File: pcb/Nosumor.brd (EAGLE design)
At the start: 50 x 50 mm, 111 parts, among them IC1 STM32F722RET, IC2 REG1117, IC3 TPS77018, J3 SJ-43515TS-SMT-EDGE, K1 CHERRY-MX, K2 CHERRY-MX, K3 KSC623J, K4 KSC623J, K5 KSC623J, Q1 CX2016DB, Q2 ABMM-6.000MHZ, Q3 FDY100PZ, Q4 FDY100PZ, Q5 FDY100PZ, Q6 FDY100PZ, U2 USB3370, U3 TLV320AIC3110

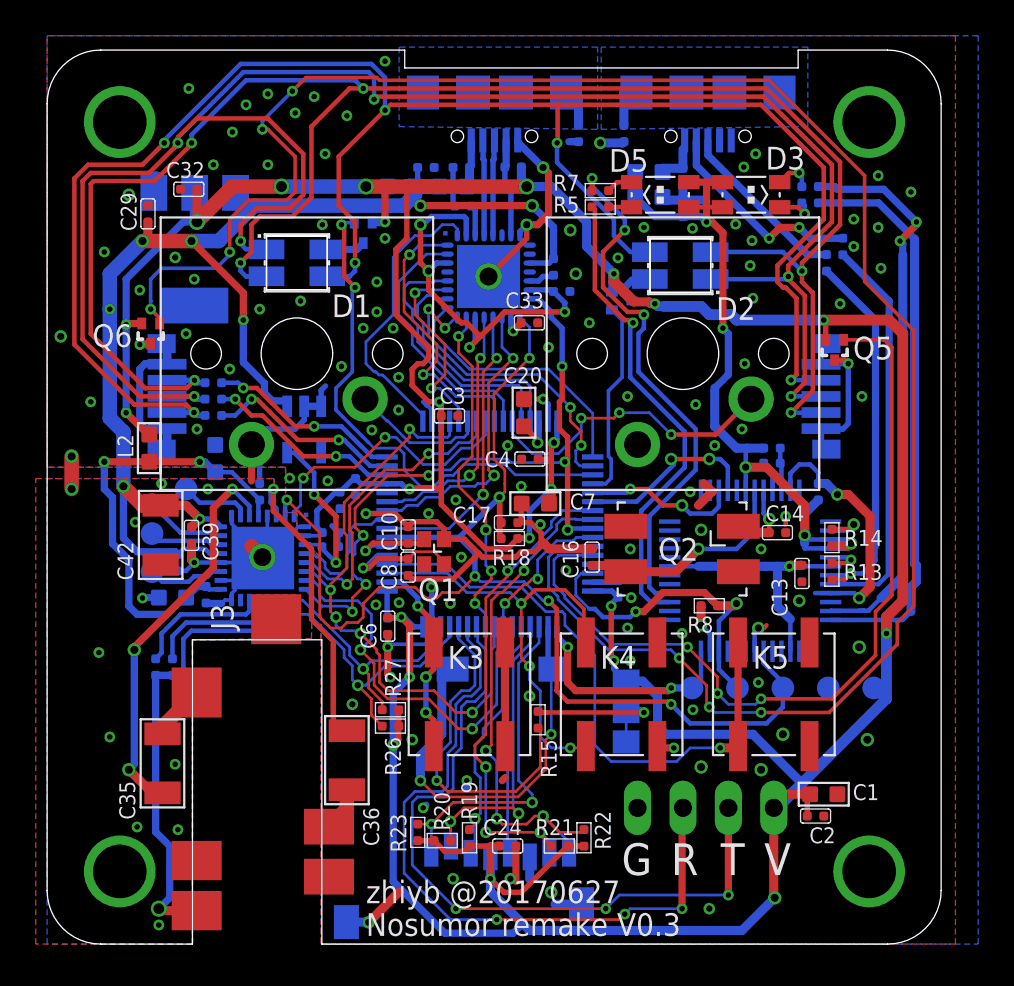
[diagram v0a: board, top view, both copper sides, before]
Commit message: PCB: Connections done, update revision to 1.0
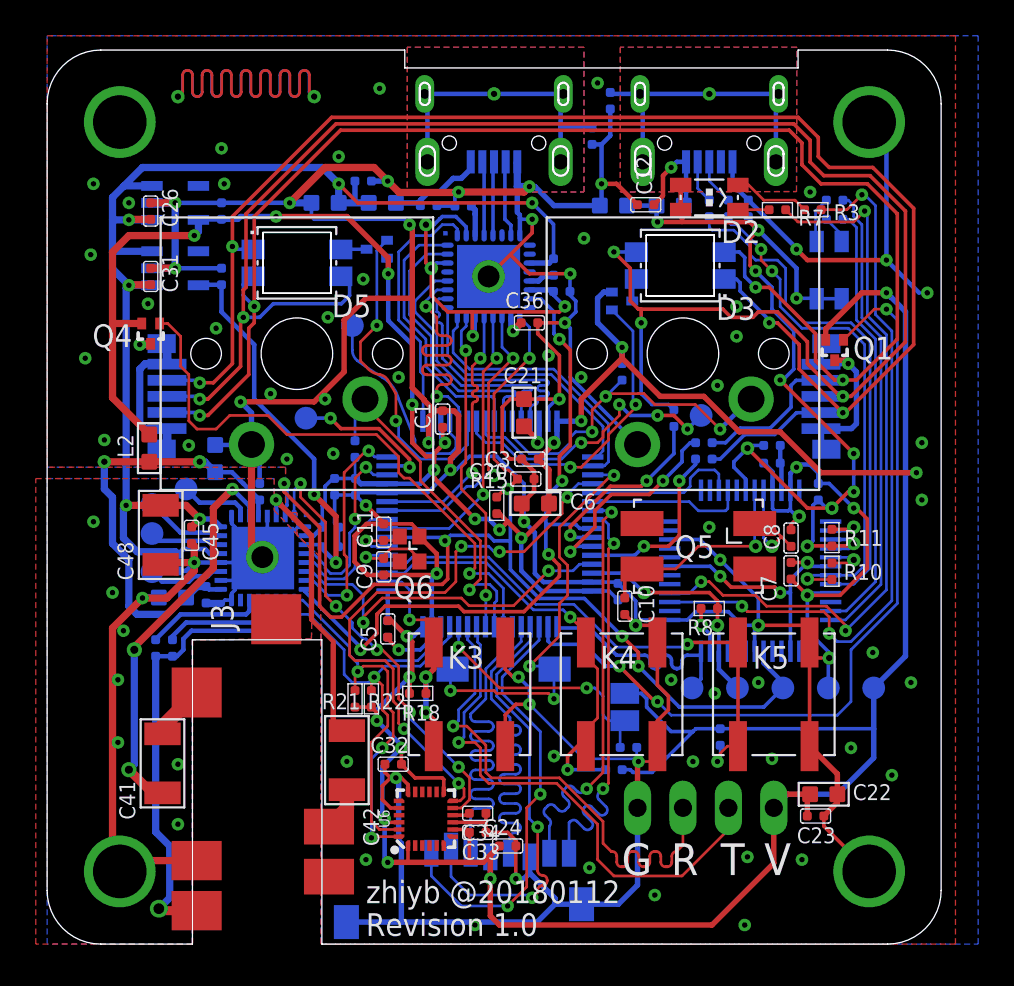
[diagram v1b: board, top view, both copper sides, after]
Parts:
- removed BOOT: 0R-JUMPB, jump-0r-smd:B0R-JMP
- removed IC2: REG1117, burr-brown:SOT223
- removed IC3: TPS77018, texas:SOT23-DBV
- removed R26, R27, R31: 2.2K, Seeed-Resistor:R0402
- removed R28, R30: 10K 1/16W, Seeed-Resistor:R0402
- added A1, A2, D: TPB1,27, testpad:B1,27
- added C45, C46, C47, C49: 100nf, Seeed-Capacitor:C0402
- added C48: 100uf, Seeed-Capacitor:C1206
- added R1, R3: 330R, Seeed-Resistor:R0402
- added R2: 150R, Seeed-Resistor:R0402
- added R25: 2.2K, Seeed-Resistor:R0402
- added SJ1: (no value), jumper:SJ
- added U4: TLV320AIC3110, ti:VQFN32
- added U5: AP2112K-1.8V, SparkFun-IC-Power:SOT23-5
- added U6: 9DoF IMU, SparkFun-Sensors:QFN24-3X3
- C1, C23, C27, C37: value 10uf -> 100nf; device Seeed-Capacitor:C0603 -> Seeed-Capacitor:C0402
- C10, C8: value 12pf -> 18pf
- C11: value 10nf -> 12pf
- C12: value 1UF 6.3V -> 100nf
- C13: value 33nf -> 100nf
- C14: value 18pf -> 10nf
- C16: value 18pf -> 100nf
- C17, C26, C31, C38: value 100nf -> 1UF 6.3V
- C18, C22, C28, C43, C44: value 100nf -> 10uf; device Seeed-Capacitor:C0402 -> Seeed-Capacitor:C0603
- C20: value 4.7uf -> 100nf; device Seeed-Capacitor:C0603 -> Seeed-Capacitor:C0402
- C21, C6: value 100nf -> 4.7uf; device Seeed-Capacitor:C0402 -> Seeed-Capacitor:C0603
- C33: value 1UF 6.3V -> 10nf
- C34: value 470nf -> 100nf
- C35, C36: value 100uf -> 1UF 6.3V; device Seeed-Capacitor:C1206 -> Seeed-Capacitor:C0402
- C40: value 10uf -> 470nf; device Seeed-Capacitor:C0603 -> Seeed-Capacitor:C0402
- C41: value 100nf -> 100uf; device Seeed-Capacitor:C0402 -> Seeed-Capacitor:C1206
- C7: value 4.7uf -> 33nf; device Seeed-Capacitor:C0603 -> Seeed-Capacitor:C0402
- C9: value 100nf -> 12pf
- D1, D2: value HSMF-A3-BACK -> APBD3224SURKCGKC-F01; device led:HSMF-A3-BACK -> led:1210
- D3, D5: value APBD3224SURKCGKC-F01 -> HSMF-A3-BACK; device led:1210 -> led:HSMF-A3-BACK
- J1, J4: device Wurth_Elektronik_Electromechanic_Input-Output_Connectors_rev17b:629105136821 -> Wurth_Elektronik_Electromechanic_Input-Output_Connectors_rev16b:629105150521
- Q1: value CX2016DB -> FDY100PZ; device crystal:CX2016DB -> transistor:SC-89
- Q2: value ABMM-6.000MHZ -> FDY100PZ; device crystal:ABMM -> transistor:SC-89
- Q5: value FDY100PZ -> ABMM-6.000MHZ; device transistor:SC-89 -> crystal:ABMM
- Q6: value FDY100PZ -> CX2016DB; device transistor:SC-89 -> crystal:CX2016DB
- R10: value 150R -> 1.5K
- R11: value 150R -> 10K 1/16W
- R12: value 150R -> 22R
- R13: value 1.5K -> 22R
- R16, R17: value 22R -> 10K 1/16W
- R19, R20, R23: value 47K -> 10K 1/16W
- R21, R22: value 47K -> 2.2K
- R4, R6: value 330R -> 150R
- U2: value USB3370 -> AP2112K-3.3V; device microchip:QFN32 -> SparkFun-IC-Power:SOT23-5
- U3: value TLV320AIC3110 -> USB3370; device ti:VQFN32 -> microchip:QFN32
- moved R10 36.2 mm to (43.9, 20.9), flipped to the top, turned to 0 degrees
- moved C23 35.9 mm to (43.0, 7.16), flipped to the top, turned to 270 degrees
- moved R11 35.5 mm to (43.9, 22.7), flipped to the top, turned to 0 degrees
- moved R23 35.1 mm to (23.3, 41.3), flipped to the bottom, turned to 270 degrees
- moved C35 34.6 mm to (28.8, 36.5), flipped to the bottom
- moved C32 34.1 mm to (19.4, 10.1)
- moved C15 31.9 mm to (31.5, 47.2)
- moved R12 30.1 mm to (37.0, 41.1), turned to 180 degrees
- moved C1 29.9 mm to (22.1, 29.4), turned to 0 degrees
- moved D1 29.8 mm to (43.7, 37.7), flipped to the bottom, turned to 0 degrees
- moved R16 29.5 mm to (17.2, 27.7), turned to 0 degrees
- moved C40 29.2 mm to (6.07, 16.6), turned to 0 degrees
- moved C19 28.7 mm to (19.1, 17.6), turned to 180 degrees
- moved C33 28.6 mm to (24.1, 6.25)
- moved C36 26.5 mm to (27.0, 34.7)
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- renumbered 3V3 to VDD, R29 to R24, SLM to TP10, SLP to TP9, SRM to TP12, SRP to TP11, UART to JP1
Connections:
- removed net AIC_SCL: IC1.61, R26.1, U3.10
- removed net AIC_SDA: IC1.62, R27.1, U3.9
- removed net N$15: R16.1, U1.8
- removed net N$16: J1.3, R17.2
- removed net N$22: C21.2, J1.SHELL, J1.SHELL1, J1.SHELL2, J1.SHELL3
- removed net N$40: D1.3, D2.3, D4.5, D6.5, R12.2
- removed net N$41: D1.1, D2.1, D4.4, D6.4, R11.2
- removed net N$42: D1.4, D2.4, D4.3, D6.3, R10.2
- removed net N$51: C27.2, C28.2, C31.2, C37.2, L2.1, U3.17, U3.28
- removed net N$8: J1.2, R16.2
- removed net N$9: R13.2, R17.1, U1.7
- removed net NC1: IC1.45
- removed net RGB2_B: IC1.16, R10.1
- removed net RGB2_G: IC1.15, R12.1
- removed net RGB2_R: IC1.14, R11.1
- new net ADC1: A1.TP, IC1.15
- new net ADC2: A2.TP, IC1.24
- new net AVDD: C28.2, C29.2, C37.2, C43.2, L2.1, U4.17, U4.28
- new net DAC: D.TP, IC1.20
- new net DBG_BM_U: J1.2, R12.2
- new net DBG_DM: R12.1, U1.8
- new net DBG_DP: R10.2, R13.1, U1.7
- new net DBG_DP_U: J1.3, R13.2
- new net I2C_SCL: IC1.61, R21.1, U4.10, U6.23
- new net I2C_SDA: IC1.62, R22.1, U4.9, U6.24
- new net LED_B: IC1.44, R2.1
- new net LED_G: IC1.43, R6.1
- new net LED_R: IC1.42, R4.1
- new net MPU_INT: IC1.36, U6.12
- new net N$47: C34.2, U6.10
- new net RGB_B: D3.1, D4.3, D5.1, D6.3, R2.2
- new net RGB_G: D3.4, D4.5, D5.4, D6.5, R6.2
- new net RGB_R: D3.3, D4.4, D5.3, D6.4, R4.2
- net +1V8: now also C27.2, C38.2, U4.3, U5.5; no longer C26.2, IC3.5, U3.3
- net +3V3: now also C14.2, C17.2, C19.2, C22.2, C23.2, C30.2, C33.2, Q1.3, Q2.3, R15.2, R16.2, R17.2, R21.2, R22.2, SJ1.1, U2.5, U4.2, U6.1, U6.13, U6.22, U6.8; no longer BOOT.1, C11.2, C12.2, C15.2, C2.2, C7.2, IC2.2, Q5.3, Q6.3, R21.1, R22.1, R23.2, R26.2, R27.2, R30.2, U3.2
- net +5V: now also C26.2, C31.2, C44.2, C45.2, C46.2, C48.2, U2.1, U2.3, U3.11, U4.21, U4.24, U5.1, U5.3; no longer C29.2, C38.2, C40.2, C41.2, C42.2, IC2.3, IC3.1, U2.11, U3.21, U3.24
- net AIC_BCLK: now also IC1.16, U4.7; no longer IC1.42, IC1.55, U3.7
- net AIC_DIN: now also IC1.9, U4.5; no longer IC1.23, U3.5
- net AIC_DOUT: now also IC1.14, U4.4; no longer IC1.9, U3.4
- net AIC_GPIO: now also U4.32, U6.11; no longer IC1.24, U3.32
- net AIC_WCLK: now also IC1.45, U4.6; no longer IC1.20, IC1.56, U3.6
- net BOOT0: now also R14.1, SJ1.2; no longer R15.1
- net DBG_5V: now also C13.2, C16.2, C18.2, D1.1, D1.3, D2.1, D2.3, R11.2; no longer C19.2, C22.2, C23.2, D3.1, D3.3, D5.1, D5.3, R14.2
- net DBG_SWD_LED1: now also R5.1; no longer R6.1
- net DBG_SWD_LED2: now also R1.1; no longer R4.1
- net DBG_TX_LED: now also R3.1; no longer R5.1
- net GND: now also C13.1, C2.2, C34.1, C35.1, C36.1, C45.1, C46.1, C47.1, C48.1, C49.1, C7.2, C9.1, Q6.2, R14.2, R23.1, U2.2, U3.8, U4.1, U4.16, U4.18, U4.20, U4.25, U4.29, U4.EXP, U5.2, U6.18, U6.20, U6.9; no longer BOOT.3, C13.2, C2.1, C40.1, C41.1, C42.1, C7.1, C9.2, IC2.1, IC3.2, IC3.3, Q1.2, R28.1, U2.8, U2.EXP, U3.1, U3.16, U3.18, U3.20, U3.25, U3.29
- net KEY_1: now also IC1.56, R16.1; no longer IC1.22
- net KEY_2: now also R17.1
- net KEY_3: now also R18.1
- net KEY_4: now also R19.1
- net KEY_5: now also R20.1
- net LED_1: now also IC1.22; no longer IC1.35
- net LED_2: now also IC1.23, Q2.1; no longer IC1.36, Q4.1
- net LED_3: now also IC1.50, Q1.1; no longer IC1.44, Q5.1
- net LED_4: now also IC1.55, Q4.1; no longer IC1.43, Q6.1
- net MCLK: now also U3.15, U4.8; no longer U2.15, U3.8
- net MMC_CD: now also IC1.35; no longer IC1.50
- net MMC_CMD: no longer R19.1
- net MMC_D0: no longer R21.2
- net MMC_D1: no longer R22.2
- net MMC_D2: no longer R23.1
- net MMC_D3: no longer R20.1
- net N$1: now also C41.2; no longer C35.2
- net N$10: now also C7.1; no longer C13.1
- net N$11: now also C2.1; no longer C9.1
- net N$12: now also D1.4, R5.2; no longer D3.4, R6.2
- net N$13: now also C12.2; no longer C18.2
- net N$14: now also R10.1; no longer R13.1
- net N$17: now also R11.1; no longer R14.1
- net N$18: now also C8.2, Q5.1; no longer C14.2, Q2.1
- net N$19: now also C10.2, Q5.3; no longer C16.2, Q2.3
- net N$2: now also C42.2; no longer C36.2
- net N$20: now also D2.4; no longer D5.4
- net N$21: now also D2.2, R3.2; no longer D5.2, R5.2
- net N$23: now also D1.2, R1.2; no longer D3.2, R4.2
- net N$24: now also C9.2, Q6.1; no longer C8.2, Q1.1
- net N$26: now also C11.2, Q6.3; no longer C10.2, Q1.3
- net N$27: now also C15.2, J1.Z1, J1.Z2, J1.Z3, J1.Z4; no longer BOOT.2, R15.2
- net N$28: now also Q4.2; no longer Q6.2
- net N$29: now also C21.2; no longer C20.2
- net N$3: now also C40.2, R25.2, U4.11; no longer C34.2, R31.2, U3.11
- net N$30: now also U4.19; no longer U3.19
- net N$31: now also C47.2; no longer C43.2
- net N$32: now also U3.13; no longer U2.13
- net N$33: now also C35.2, U3.14, U3.2, U3.22, U3.30; no longer C30.2, U2.14, U2.2, U2.22, U2.30
- net N$34: now also D5.2; no longer D1.2
- net N$35: now also C49.2, J4.Z1, J4.Z2, J4.Z3, J4.Z4; no longer C44.2, J4.SHELL, J4.SHELL1, J4.SHELL2, J4.SHELL3
- net N$36: now also C36.2, U3.18; no longer C33.2, U2.18
- net N$37: now also R23.2, U3.3; no longer R28.2, U2.3
- net N$38: now also Q1.2; no longer Q5.2
- net N$39: now also D3.2, Q2.2; no longer D2.2, Q4.2
- net N$4: now also J4.2, U3.4; no longer J4.3, U2.5
- net N$44: now also U4.26; no longer U3.26
- net N$45: now also U4.23; no longer U3.23
- net N$46: now also C40.1, U4.14; no longer C34.1, U3.14
- net N$48: now also C42.1, U4.30; no longer C36.1, U3.30
- net N$49: now also R25.1, U4.12; no longer R31.1, U3.12
- net N$5: now also J4.3, U3.5; no longer J4.2, U2.4
- net N$50: now also C41.1, U4.27; no longer C35.1, U3.27
- net N$6: now also U3.7; no longer R30.1, U2.7
- net N$7: now also U4.22; no longer U3.22
- net SRST_N: now also C20.2, R15.1, U3.17, U4.31; no longer C17.2, R18.1, U2.17, U3.31
- net ULPI_CLK: now also U3.27; no longer U2.27
- net ULPI_D0: now also U3.1; no longer U2.1
- net ULPI_D1: now also U3.32; no longer U2.32
- net ULPI_D2: now also U3.31; no longer U2.31
- net ULPI_D3: now also U3.28; no longer U2.28
- net ULPI_D4: now also U3.26; no longer U2.26
- net ULPI_D5: now also U3.25; no longer U2.25
- net ULPI_D6: now also U3.24; no longer U2.24
- net ULPI_D7: now also U3.23; no longer U2.23
- net ULPI_DIR: now also U3.19; no longer U2.19
- net ULPI_NXT: now also U3.21; no longer U2.21
- net ULPI_STP: now also U3.20; no longer U2.20
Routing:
- net GND: track 131.7 -> 414.5 mm, vias 129 -> 98
- net N$40: track 106.6 -> 0.00 mm, vias 6 -> 0
- net N$41: track 104.7 -> 0.00 mm, vias 6 -> 0
- net N$42: track 103.4 -> 0.00 mm, vias 6 -> 0
- net RGB_R: track 0.00 -> 102.6 mm, vias 0 -> 5
- net RGB_B: track 0.00 -> 89.3 mm, vias 0 -> 4
- net RGB_G: track 0.00 -> 89.1 mm, vias 0 -> 4
- net LED_4: track 112.6 -> 32.7 mm, vias 7 -> 1
- net N$22: track 2.52 -> 47.7 mm, vias 0 -> 2
- net MPU_INT: track 0.00 -> 32.6 mm, vias 0 -> 5
- net DBG_DP: track 0.00 -> 29.3 mm, vias 0 -> 3
- net DBG_DM: track 0.00 -> 28.9 mm
- net I2C_SDA: track 0.00 -> 26.2 mm, vias 0 -> 3
- net N$51: track 25.2 -> 0.00 mm, vias 2 -> 0
- net AVDD: track 0.00 -> 25.2 mm, vias 0 -> 2
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- added copper zone on layer 1, net N$27
- added copper zone on layer 16, net N$27
- added copper zone on layer 1, net N$35
- removed copper zone on layer 16, net N$22
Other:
- board text added: "Revision 1.0"
- board text added: "zhiyb @20180112"
- board text removed: "Nosumor remake V0.3"
- board text removed: "OwO"
- board text removed: "zhiyb @20170627"

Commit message: PCB: Revision 1.0, silkscreen checked
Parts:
- removed TP11, TP12: TPB1,27, testpad:B1,27
- added GND$2, SCL, SDA, SRM, SRP: TPB1,27, testpad:B1,27
- moved C28 0.61 mm to (6.40, 19.4)
- moved C29 0.36 mm to (8.53, 19.5)
- moved C43 0.30 mm to (9.09, 27.2)
- moved R20 0.30 mm to (37.3, 11.6)
- renumbered SJ1 to BOOT, TP10 to SLM, TP9 to SLP
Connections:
- net GND: now also GND$2.TP
- net I2C_SCL: now also SCL.TP
- net I2C_SDA: now also SDA.TP
- net N$44: now also SRP.TP; no longer TP11.TP
- net N$45: now also SRM.TP; no longer TP12.TP
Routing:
- net I2C_SDA: track 26.2 -> 34.4 mm, vias 3 -> 4
- net I2C_SCL: track 25.1 -> 33.3 mm, vias 1 -> 2
- net GND: track 414.5 -> 417.1 mm, vias 98 -> 102
- net KEY_3: track 12.7 -> 11.8 mm, vias 3 -> 2
- net AVDD: track 25.2 -> 25.8 mm
- net UART_TX: track 29.6 -> 29.1 mm
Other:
- board text added: "C"
- board text added: "D"

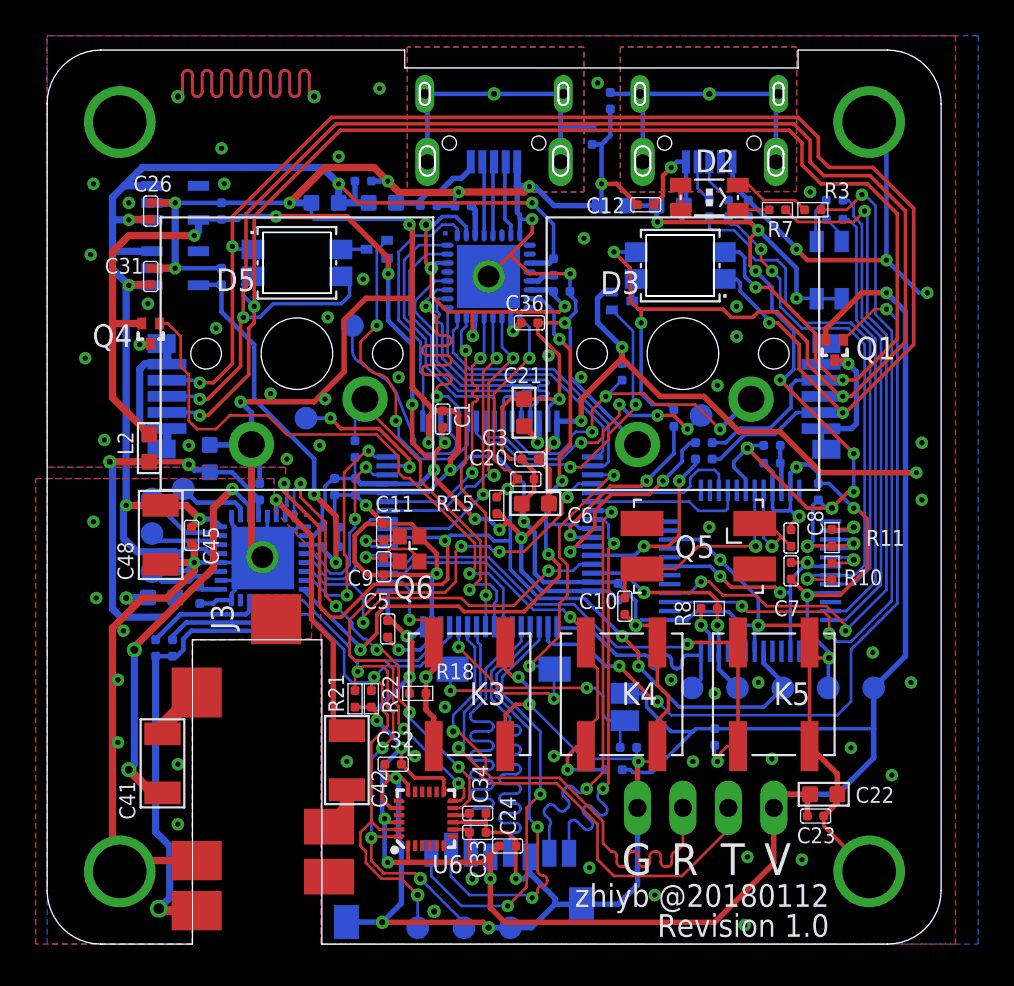
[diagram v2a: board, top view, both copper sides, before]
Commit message: PCB: Move a few things around (power supply rails)
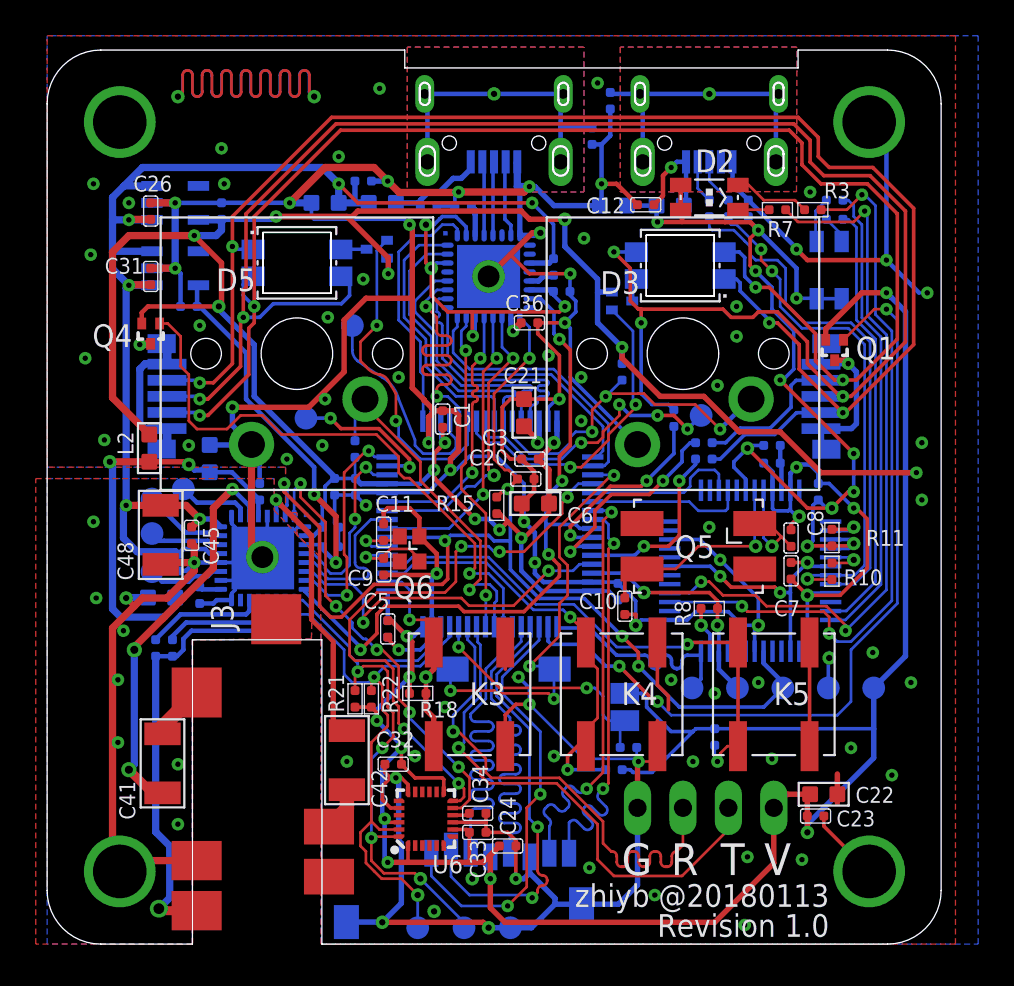
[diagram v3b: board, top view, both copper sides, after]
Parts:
- moved C38 2.48 mm to (7.92, 35.7), turned to 270 degrees
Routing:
- net +3V3: track 241.7 -> 267.4 mm, vias 21 -> 22
- net GND: track 417.1 -> 402.0 mm
- net AIC_DIN: track 7.52 -> 8.86 mm
- net +1V8: track 21.9 -> 21.3 mm
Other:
- board text added: "zhiyb @20180113"
- board text removed: "zhiyb @20180112"

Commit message: PCB: Conform to a more restrict design rule
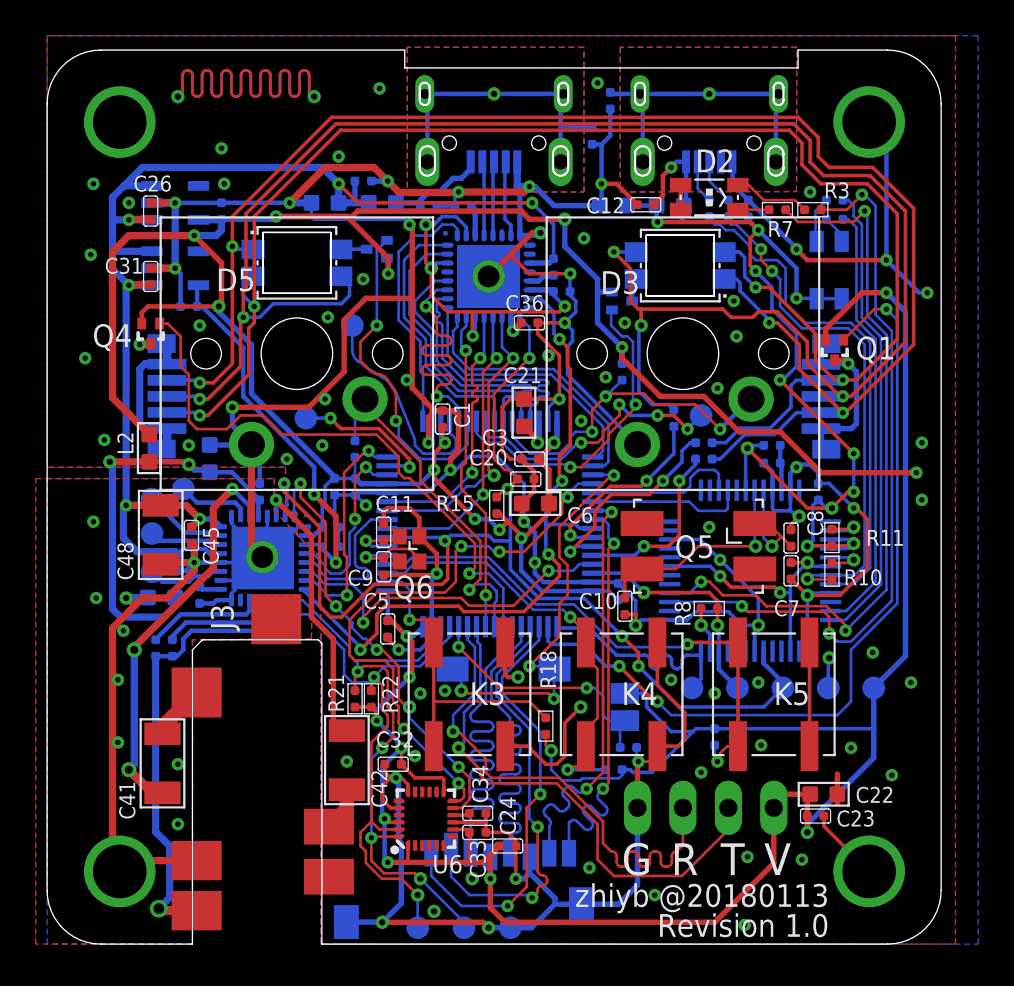
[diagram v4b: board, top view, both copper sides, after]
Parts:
- moved R18 7.39 mm to (27.9, 12.2), turned to 0 degrees
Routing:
- net KEY_3: track 11.8 -> 18.1 mm, vias 2 -> 1
- net +3V3: track 267.4 -> 273.4 mm, vias 22 -> 23
- net GND: track 402.0 -> 399.8 mm, vias 102 -> 103
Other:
- outline, holes or cut-outs redrawn
